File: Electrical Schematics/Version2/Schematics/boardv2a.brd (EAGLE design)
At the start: 188.8 x 159.4 mm, 560 parts, among them IC1 MCP41HVX1ST, IC2 ADUM4160BRW, IC3 SE555D, IC5 74LVC1G04DBV, IC6 74LVC1G04DBV, IC7 4030D, K1 G5V-2, Q1 IRLML2060TRPBFBSS123LT1G, Q10 IRLML2060TRPBFBSS123LT1G, Q11 IRLML2060TRPBFBSS123LT1G, Q13 IRLML2060TRPBFBSS123LT1G, Q14 IRLML2060TRPBFBSS123LT1G, Q15 IRLML2060TRPBFBSS123LT1G, Q16 IRLML2060TRPBFBSS123LT1G, Q17 IRLML2060TRPBFBSS123LT1G, Q18 BSP170P, Q19 IRLML2060TRPBFBSS123LT1G, Q2 IRLML2060TRPBFBSS123LT1G, Q3 IRLML2060TRPBFBSS123LT1G, Q4 BSP170P, Q5 IRLML2060TRPBFBSS123LT1G, Q6 IRLML2060TRPBFBSS123LT1G, Q7 ASFL1, Q8 IRLML2060TRPBFBSS123LT1G, Q9 IRLML2060TRPBFBSS123LT1G, U1 CP2130-GM, U10 SN65HVDA100-Q1_D_8, U11 ADUM3442CRWZ, U12 ADUM3442CRWZ, U13 ADUM3442CRWZ, U14 ADUM3442CRWZ, U15 ADUM3442CRWZ, U16 ADUM3442CRWZ, U17 ADUM3442CRWZ, U18 LM1085_KTT_3, U19 ADUM3442CRWZ, U2 TMS570LS0432_PZ_100, U20 ADUM3442CRWZ, U3 LM1085_KTT_3, U4 LM1085_KTT_3, U5 LM1084_KTT_3, U6 TPS3514_D_14, U7 LM1085_KTT_3, U9 ADUM3442CRWZ, X4 5566-4

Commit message: updated changes
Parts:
- moved C84 98.6 mm to (22.4, 50.0), turned to 270 degrees
- moved C85 88.1 mm to (30.4, 49.7), turned to 180 degrees
- moved C109 83.7 mm to (26.7, 55.4), turned to 270 degrees
- moved JP12 69.4 mm to (117.2, -26.9)
- moved LED6 59.3 mm to (124.7, 74.4)
- moved C74 58.9 mm to (26.4, 71.5)
- moved C75 58.0 mm to (27.2, 67.4)
- moved R39 57.3 mm to (118.6, 72.5)
- moved TP71 34.2 mm to (64.6, 31.9)
- moved C76 34.0 mm to (17.8, 69.2), turned to 90 degrees
- moved C43 24.6 mm to (7.87, 59.4), turned to 270 degrees
- moved C45 24.1 mm to (7.37, 65.7)
- moved C10 22.5 mm to (135.8, 88.5), turned to 180 degrees
- moved JP18 17.3 mm to (40.4, 49.5)
- moved JP13 16.6 mm to (40.3, 53.5)
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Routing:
- net N$204: track 43.8 -> 0.00 mm, vias 1 -> 0
- net ETHERNET_3.3_J_+: track 41.3 -> 0.00 mm
- net N$205: track 40.9 -> 0.00 mm, vias 1 -> 0
- net 0.1: track 38.3 -> 0.00 mm
- net N$202: track 35.7 -> 0.00 mm, vias 2 -> 0
- net N$199: track 23.2 -> 0.00 mm, vias 2 -> 0
- net N$203: track 21.1 -> 0.00 mm
- net GNDA: track 17.7 -> 0.00 mm
- net N$201: track 14.5 -> 0.00 mm
- net N$207: track 13.8 -> 0.00 mm
- net WIZNET_TO_GND: track 13.3 -> 0.00 mm
- net GND: track 128.2 -> 117.3 mm, vias 17 -> 15
- net 1V8A: track 8.92 -> 0.00 mm
- net N$196: track 8.92 -> 0.00 mm
- net N$200: track 2.96 -> 0.00 mm
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
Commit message: work on lin
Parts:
- moved C107 117.1 mm to (35.4, 55.6)
- moved C95 88.8 mm to (40.5, 2.16), turned to 0 degrees
- moved R109 77.7 mm to (102.6, 92.2), turned to 0 degrees
- moved C82 28.7 mm to (-5.21, 45.2)
- moved C77 28.5 mm to (-14.1, 66.8), turned to 90 degrees
- moved C81 27.8 mm to (-11.0, 47.2)
- moved C84 24.6 mm to (-1.78, 55.0)
- moved C79 22.5 mm to (-9.91, 52.2)
- moved C110 22.0 mm to (-1.91, 46.2)
- moved R28 19.0 mm to (-8.38, 56.6)
- moved L4 18.9 mm to (-2.54, 49.4)
- moved C78 18.5 mm to (-12.2, 73.0)
- moved C2 16.8 mm to (161.9, 71.0), turned to 270 degrees
- moved C70 14.0 mm to (-3.30, 74.7)
- moved R86 13.8 mm to (-2.29, 77.7)
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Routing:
- net GND: track 117.3 -> 118.1 mm

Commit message: did more changes on placement
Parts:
- moved JP111 34.9 mm to (85.1, 42.2), turned to 0 degrees
- moved JP23 20.9 mm to (187.8, 71.4), turned to 0 degrees
- moved R95 20.2 mm to (183.6, 83.4), turned to 0 degrees
- moved TP106 18.7 mm to (103.9, 69.6)
- moved C49 14.0 mm to (96.5, 50.0), turned to 90 degrees
- moved C56 10.1 mm to (100.8, 71.0)
- moved TP115 8.57 mm to (114.3, 73.2)
- moved Q16 6.40 mm to (129.3, 50.5)
- moved R109 4.83 mm to (102.9, 87.4)
- moved Q8 3.81 mm to (109.7, 71.5)
- moved TP117 3.61 mm to (112.5, 74.5)
- moved U10 3.41 mm to (99.4, 82.5)
- moved C25 3.14 mm to (104.0, 54.0)
- moved JP2 2.95 mm to (143.0, 85.7)
- moved JP24 2.82 mm to (132.0, 93.1)
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
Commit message: updated stuff
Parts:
- removed TP143: TPB1,27, testpad:B1,27
- moved C61 82.4 mm to (122.9, 42.9), turned to 90 degrees
- moved TP100 81.8 mm to (136.5, 37.0)
- moved C44 81.3 mm to (-24.6, 83.3)
- moved R108 77.5 mm to (120.7, 42.9)
- moved TP15 77.2 mm to (-19.9, 83.9)
- moved TP113 76.8 mm to (126.6, 39.8)
- moved LED17 74.5 mm to (122.4, 39.9)
- moved C63 72.0 mm to (127.3, 46.6)
- moved C38 71.3 mm to (52.7, 70.7), turned to 270 degrees
- moved TP103 68.7 mm to (126.7, 44.3), turned to 90 degrees
- moved C53 67.2 mm to (66.4, 70.6), turned to 180 degrees
- moved C48 65.7 mm to (74.0, 69.7), turned to 90 degrees
- moved C113 64.6 mm to (59.6, 79.6), turned to 0 degrees
- moved C54 59.4 mm to (72.6, 69.6), turned to 90 degrees
- moved R94 58.7 mm to (109.9, 54.4)
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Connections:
- new net 5V_SUP_J1: JP23.2, U$2.21
- net 5V_SUPERVISED: no longer JP23.2, U$2.21
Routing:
- net CON_FNR_HIGH: track 13.4 -> 0.00 mm
- net CON_MONC_-: track 63.6 -> 61.7 mm
- net N$120: track 2.50 -> 3.86 mm
- net 3.3V_UNSUPERVISED: track 7.41 -> 6.89 mm

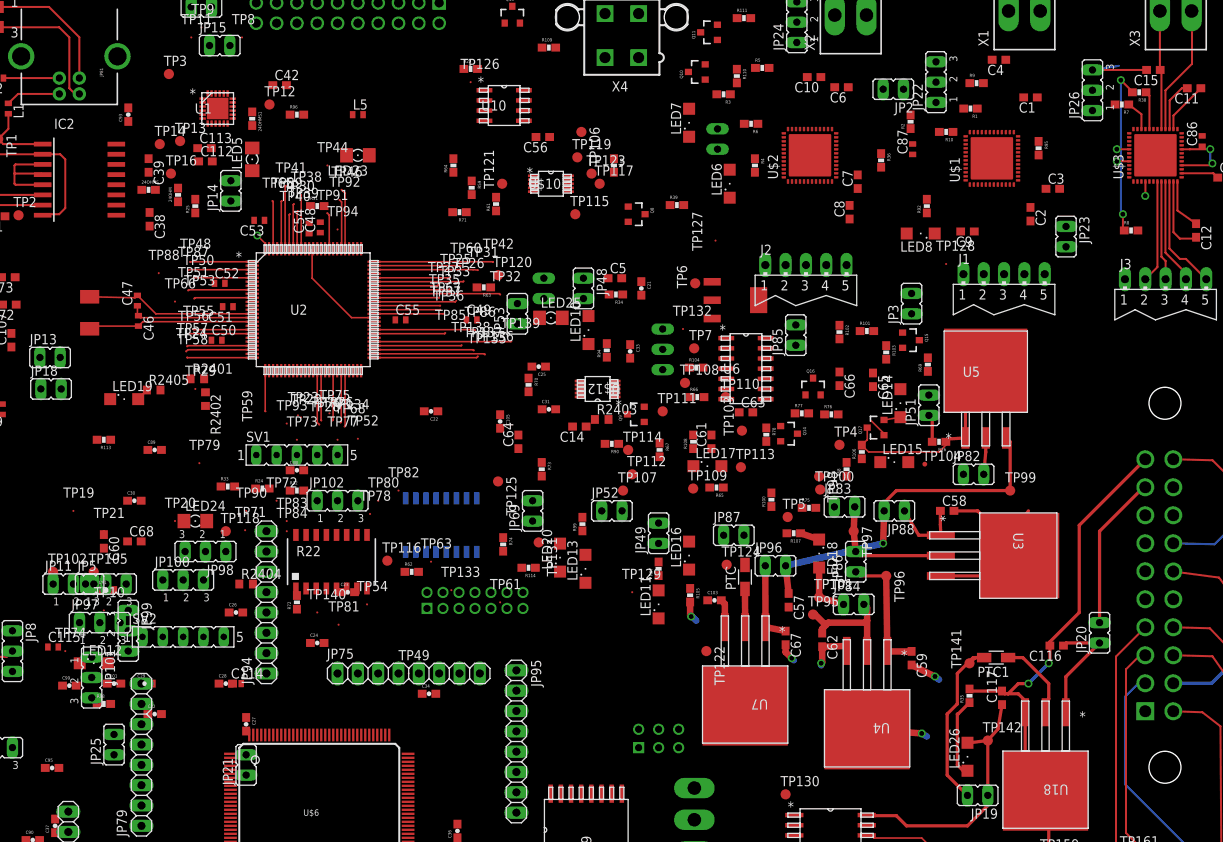
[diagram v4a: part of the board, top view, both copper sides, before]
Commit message: routed power stuff
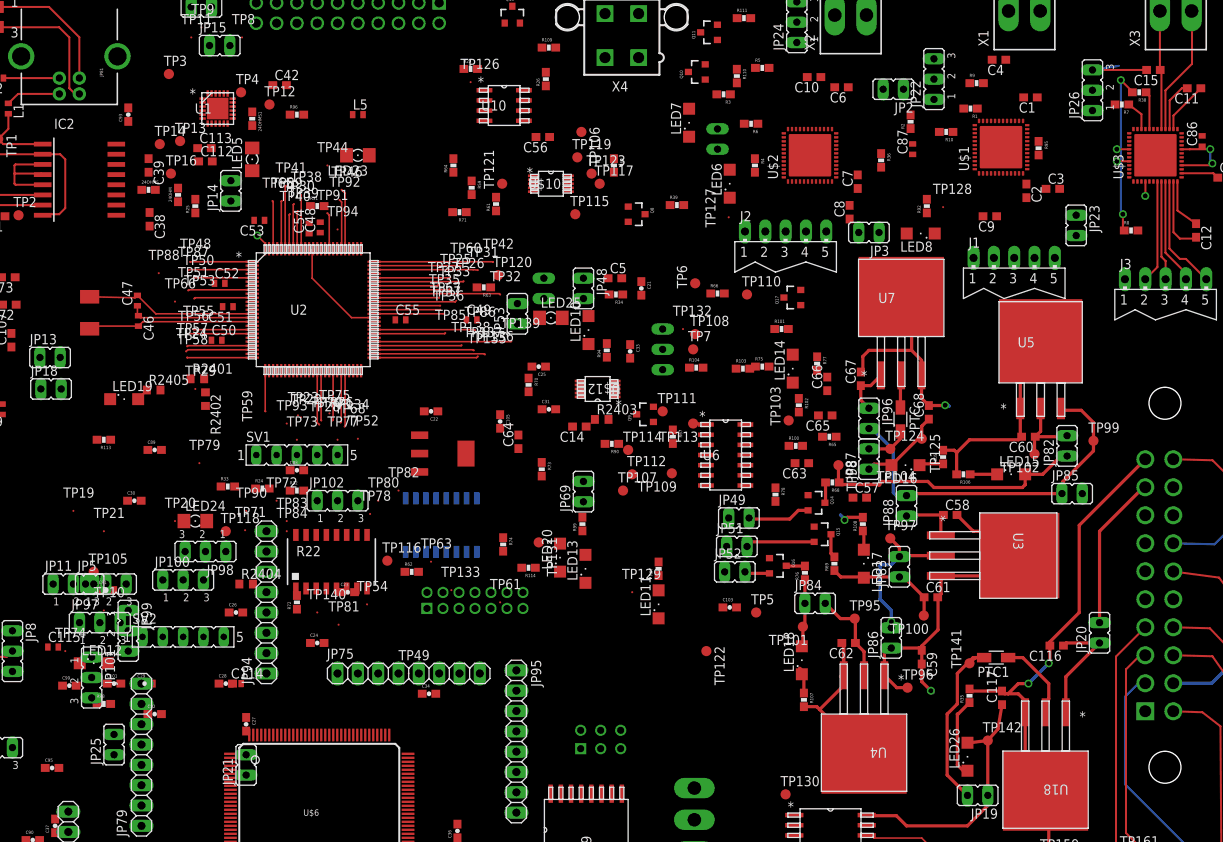
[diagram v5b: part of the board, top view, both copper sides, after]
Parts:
- moved TP102 123.6 mm to (163.3, 41.4), turned to 180 degrees
- moved C60 116.3 mm to (162.6, 43.6), turned to 180 degrees
- moved C68 100.6 mm to (150.1, 46.6), turned to 90 degrees
- moved TP4 86.8 mm to (64.1, 86.6)
- moved R26 66.9 mm to (102.2, 88.3), turned to 90 degrees
- moved U7 54.4 mm to (146.7, 60.9), turned to 0 degrees
- moved TP125 53.2 mm to (149.2, 43.3)
- moved U$11 41.3 mm to (89.4, 41.5)
- moved JP85 39.8 mm to (168.0, 36.4), turned to 270 degrees
- moved R105 36.0 mm to (151.9, 41.0), turned to 90 degrees
- moved C67 33.7 mm to (141.6, 50.8), turned to 90 degrees
- moved C61 33.6 mm to (150.4, 23.5), turned to 0 degrees
- moved JP51 29.8 mm to (126.1, 29.8), turned to 270 degrees
- moved LED16 29.3 mm to (147.2, 40.0), turned to 180 degrees
- moved PTC 27.7 mm to (146.6, 45.7), turned to 270 degrees
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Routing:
- net GND: track 118.1 -> 163.1 mm, vias 15 -> 13
- net 12V_UNSUPERVISED: track 0.00 -> 33.7 mm
- net 5V_UNSUPERVISED: track 0.00 -> 15.0 mm
- net 5V_TO_SUPERVISOR: track 0.00 -> 11.1 mm
- net N$235: track 0.00 -> 8.64 mm
- net N$163: track 0.00 -> 7.88 mm
- net N$167: track 4.56 -> 10.0 mm
- net N$174: track 0.00 -> 5.38 mm
- net N$173: track 15.9 -> 11.9 mm
- net N$177: track 10.2 -> 6.30 mm
- net 5V_SUPERVISED: track 3.48 -> 0.00 mm
- net N$242: track 0.00 -> 3.37 mm
- net N$236: track 0.00 -> 3.14 mm
- net N$249: track 0.00 -> 3.02 mm
- net 5V_SUPERVISEDB: track 0.00 -> 3.01 mm
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
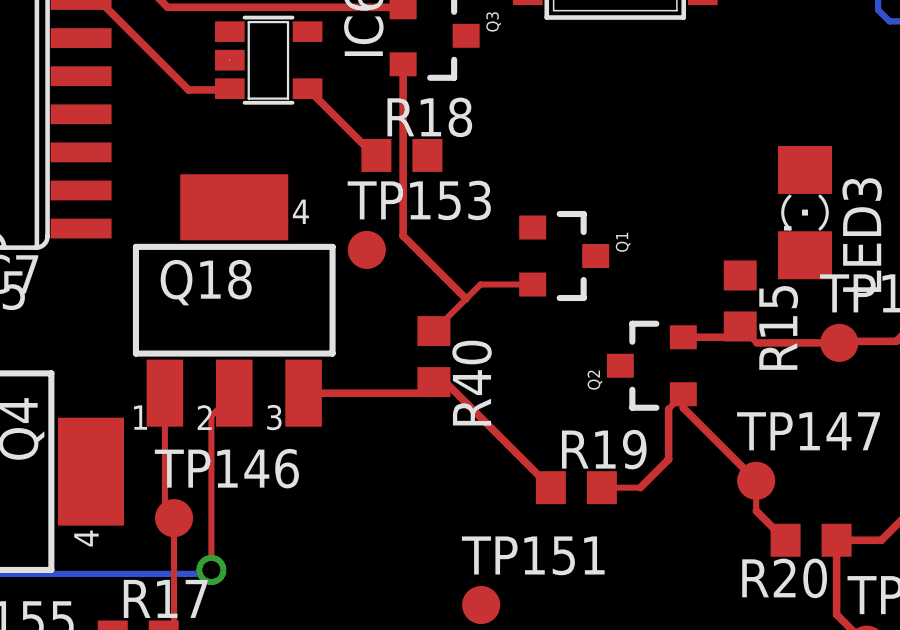
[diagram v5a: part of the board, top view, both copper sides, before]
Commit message: fixed FNR ground
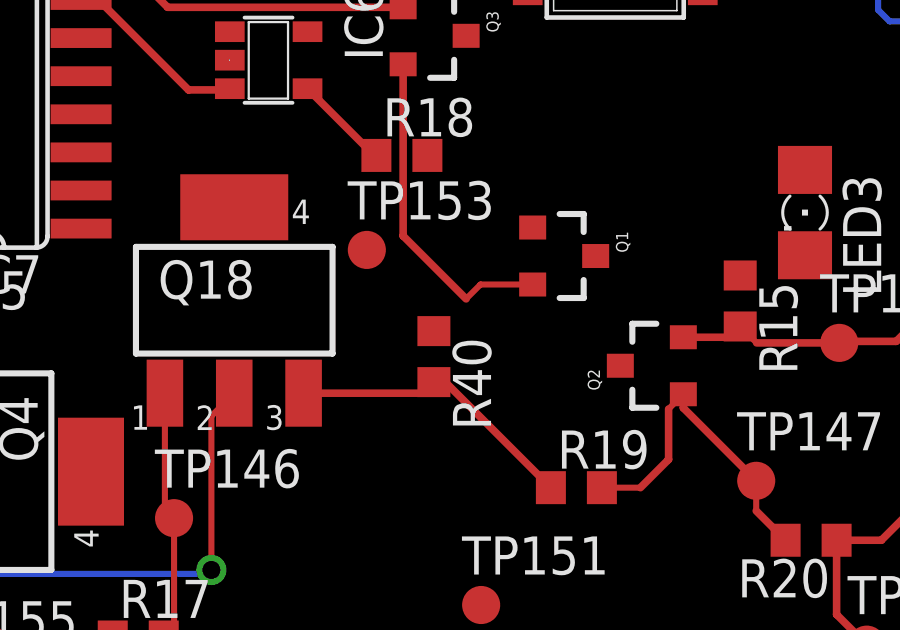
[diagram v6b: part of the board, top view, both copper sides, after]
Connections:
- net CON_NIN: now also Q1.2, Q3.2, R40.1
- net FNR_CON_GROUND: no longer Q1.2, Q3.2, R40.1
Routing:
- net FNR_CON_GROUND: track 12.6 -> 0.00 mm
- net CON_NIN: track 152.7 -> 163.8 mm
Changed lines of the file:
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@@
 <signal name="FNR_CON_GROUND">
 <contactref element="U$5" pad="P$6"/>
-<contactref element="Q3" pad="2"/>
-<contactref element="R40" pad="1"/>
-<contactref element="Q1" pad="2"/>
-<wire x1="168.8244" y1="-41.2852" x2="167.0846" y2="-41.2852" width="0.2032" layer="1"/>
-<wire x1="167.0846" y1="-41.2852" x2="166.6054" y2="-41.7644" width="0.2032" layer="1"/>
-<wire x1="166.6054" y1="-41.7644" x2="165.5318" y2="-42.838" width="0.2032" layer="1"/>
-<wire x1="164.5064" y1="-33.9446" x2="164.5064" y2="-39.6654" width="0.254" layer="1"/>
-<wire x1="164.5064" y1="-39.6654" x2="166.6054" y2="-41.7644" width="0.254" layer="1"/>
-<wire x1="164.5064" y1="-33.9446" x2="177.1676" y2="26.7436" width="0" layer="19" extent="1-1"/>
 </signal>
 <signal name="CON_MONA_+">
@@
 <wire x1="150.241" y1="-54.864" x2="149.606" y2="-54.229" width="0.254" layer="1"/>
 <wire x1="188.341" y1="-54.864" x2="158.3554" y2="-54.864" width="0.254" layer="1"/>
+<contactref element="R40" pad="1"/>
+<contactref element="Q3" pad="2"/>
+<contactref element="Q1" pad="2"/>
+<wire x1="168.8244" y1="-41.2852" x2="167.0846" y2="-41.2852" width="0.2032" layer="1"/>
+<wire x1="167.0846" y1="-41.2852" x2="166.6054" y2="-41.7644" width="0.2032" layer="1"/>
+<wire x1="164.5064" y1="-33.9446" x2="164.5064" y2="-39.6654" width="0.254" layer="1"/>
+<wire x1="164.5064" y1="-39.6654" x2="166.6054" y2="-41.7644" width="0.254" layer="1"/>
+<wire x1="166.6054" y1="-41.7644" x2="165.5318" y2="-42.838" width="0" layer="19" extent="1-1"/>
+<wire x1="156.5656" y1="-44.9072" x2="165.5318" y2="-42.838" width="0" layer="19" extent="1-1"/>
 </signal>
 <signal name="N$252">

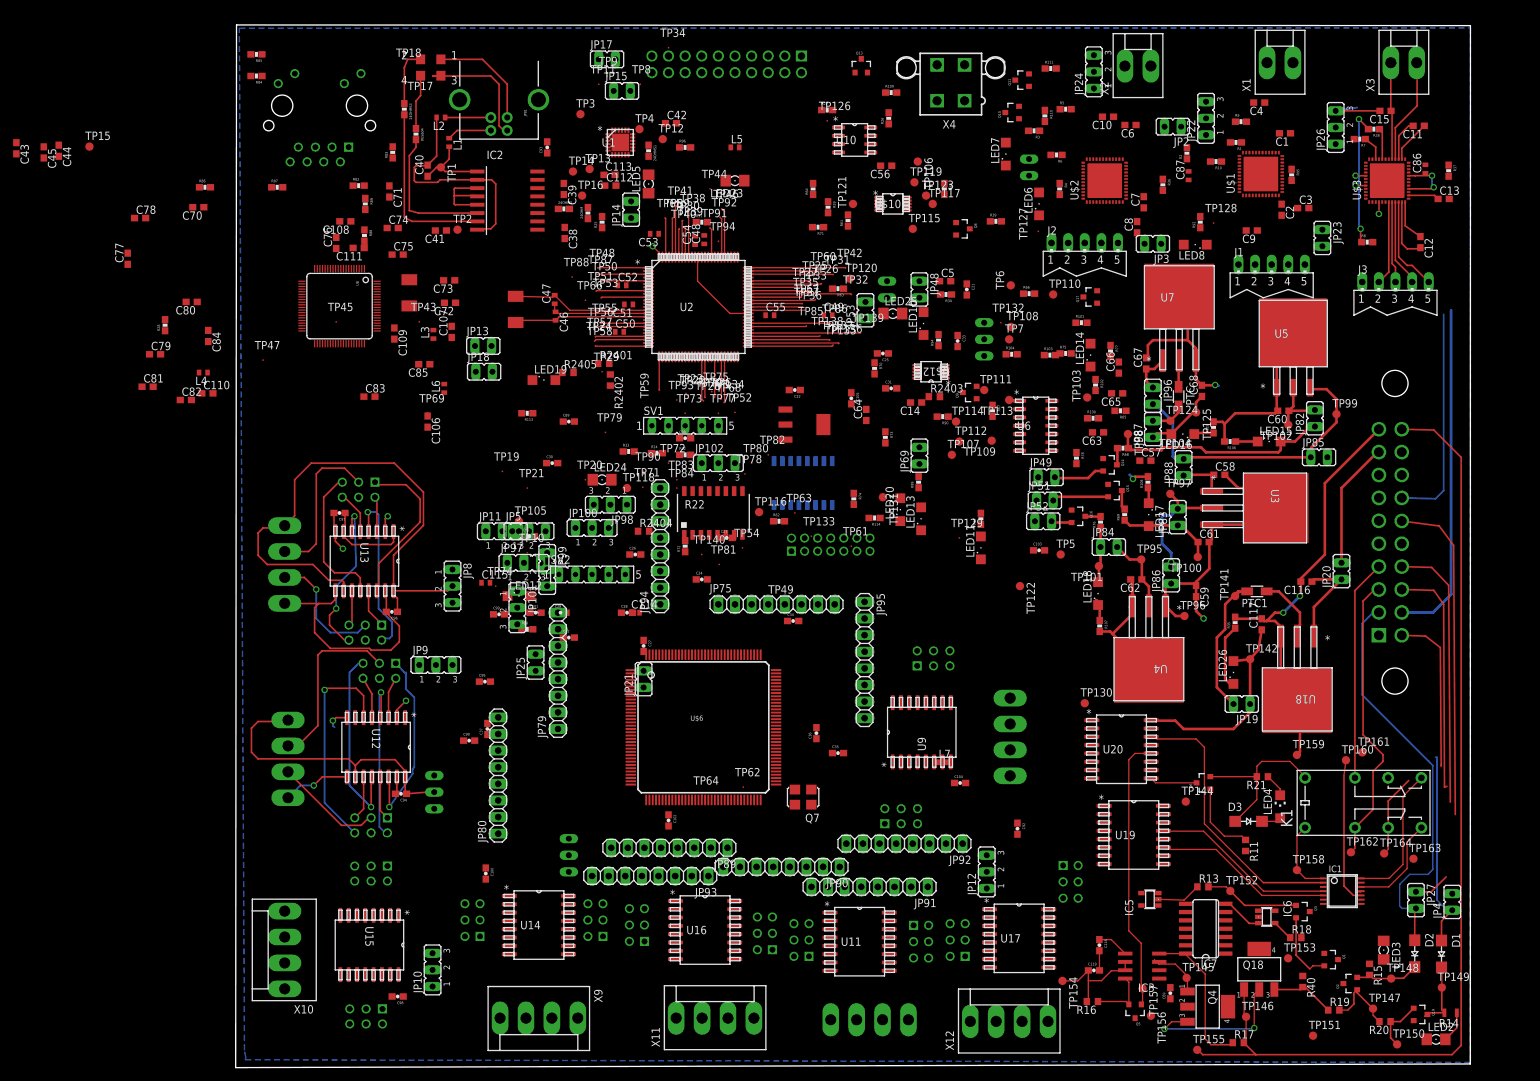
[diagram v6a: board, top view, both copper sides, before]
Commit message: routed supervisor cleaned up placement
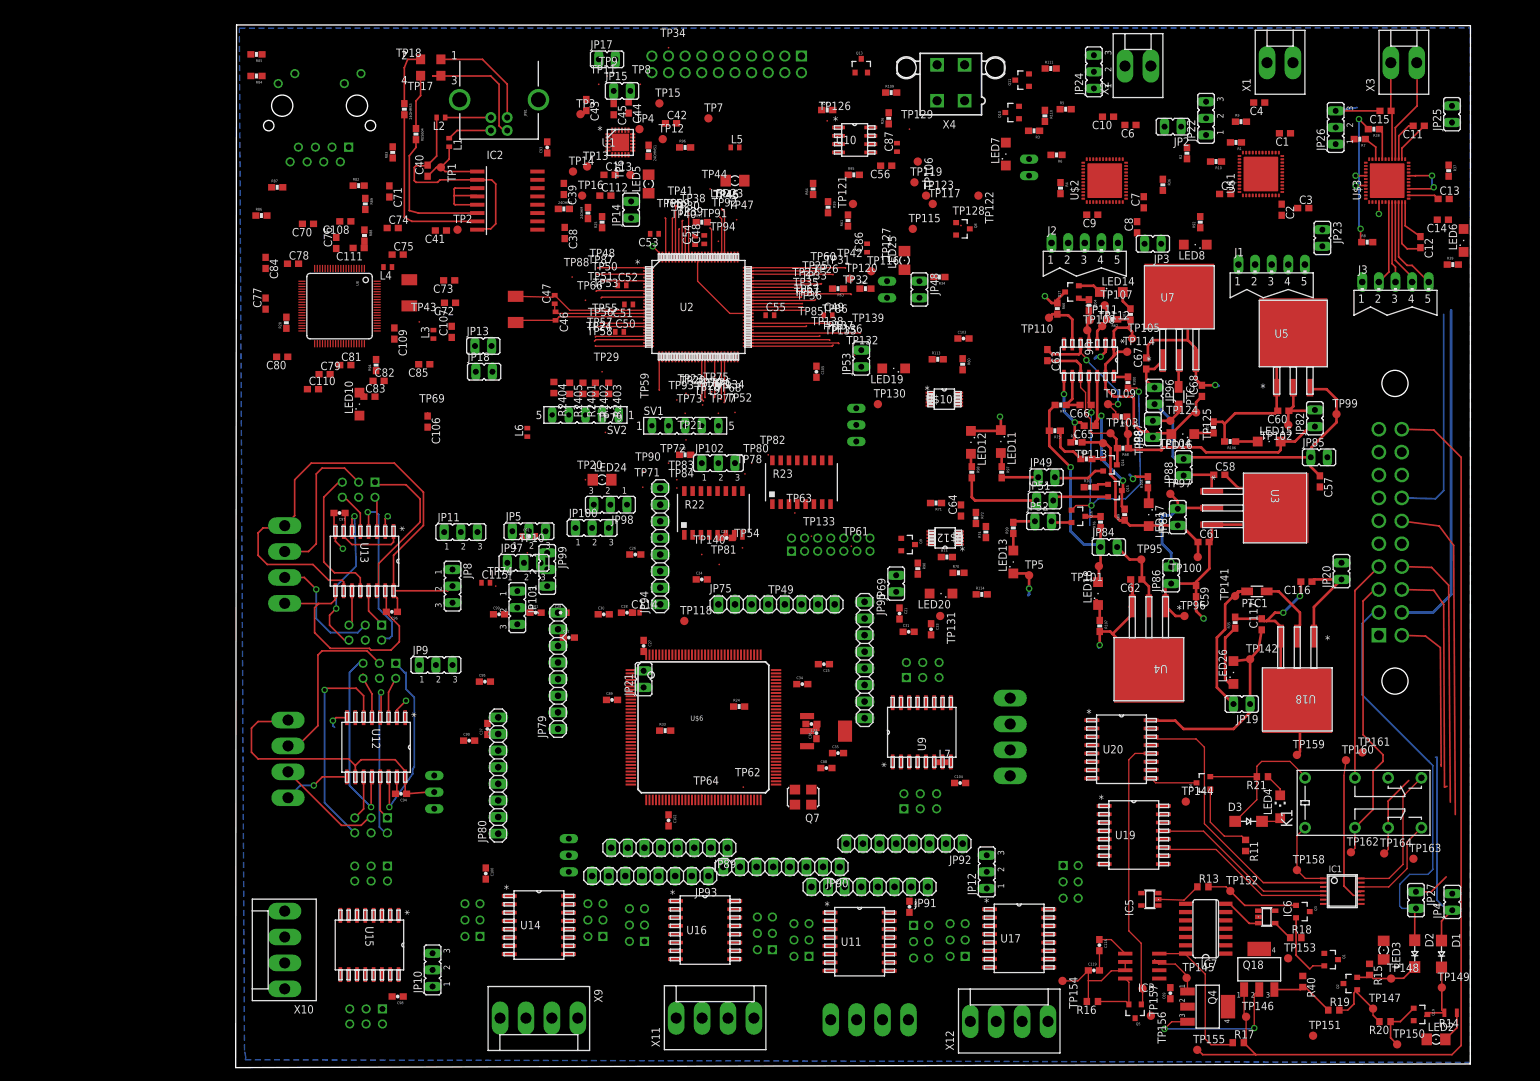
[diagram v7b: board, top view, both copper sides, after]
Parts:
- moved JP25 163.2 mm to (188.3, 88.9)
- moved TP105 97.8 mm to (139.4, 54.6)
- moved TP15 87.4 mm to (67.2, 90.6)
- moved C43 87.4 mm to (56.0, 90.3)
- moved C44 87.4 mm to (62.5, 89.9)
- moved C45 87.4 mm to (60.2, 89.7)
- moved LED10 87.1 mm to (21.3, 44.6)
- moved C86 86.2 mm to (98.9, 68.5)
- moved R94 86.1 mm to (23.9, 50.5)
- moved C14 85.2 mm to (186.9, 72.8)
- moved TP47 75.5 mm to (79.0, 72.8)
- moved LED12 73.0 mm to (114.8, 38.7), turned to 270 degrees
- moved R98 72.1 mm to (114.9, 34.2), turned to 270 degrees
- moved R39 70.2 mm to (188.5, 65.9)
- moved R95 66.9 mm to (96.9, 79.6), turned to 0 degrees
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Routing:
- net 5V_TO_SUPERVISOR: track 11.1 -> 42.9 mm
- net N$239: track 0.00 -> 28.3 mm, vias 0 -> 2
- net CON_MONB_-: track 82.2 -> 54.0 mm
- net 3.3V_UNSUPERVISED: track 8.48 -> 35.1 mm, vias 0 -> 1
- net GND: track 163.1 -> 186.4 mm, vias 13 -> 18
- net 3.3V_SUPERVISEDB: track 2.35 -> 25.3 mm, vias 0 -> 1
- net 5V_SUPERVISEDB: track 3.01 -> 25.5 mm, vias 0 -> 2
- net 12V_SUPERVISEDB: track 2.57 -> 24.7 mm
- net IS12: track 0.00 -> 21.0 mm, vias 0 -> 2
- net CON_MONB_+: track 19.4 -> 0.00 mm
- net 5V_UNSUPERVISED: track 15.0 -> 32.2 mm
- net 5V_SUPERVISED: track 0.00 -> 13.1 mm
- net IS5: track 0.00 -> 12.7 mm, vias 0 -> 2
- net POWER_GOOD_OUT: track 0.00 -> 8.59 mm
- net N$178: track 0.00 -> 7.87 mm
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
